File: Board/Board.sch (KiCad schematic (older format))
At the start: 40 parts, among them J1 5025700893, J2 Conn_01x02_Male, Q1 Q_NMOS_GSD, Q2 Q_NMOS_GSD, SW2 SW_SPST, U1 ATmega328P-AU, U2 TLV61225DCKR, Y1 10MHz

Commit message: Minor improvements
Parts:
- removed C4, C5: 18pF, Capacitor_SMD:C_0603_1608Metric, symbol Device:C
- removed R4: 3.48, Resistor_SMD:R_2512_6332Metric, symbol Device:R
- removed Y1: 10MHz, Crystal:Crystal_HC49-4H_Vertical, symbol Device:Crystal
- TP1, TP10, TP2, TP3, TP4, TP5, TP6, TP7, TP8, TP9: footprint TestPoint:TestPoint_THTPad_D1.0mm_Drill0.5mm -> Board:TestPoint_THTPad_D1.0mm_Drill0.7mm
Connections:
- net +3V3: no longer C6.1
- net +BATT: now also C6.1, LS1.1
- no-connect marks 13 -> 15
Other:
- moved on the sheet: C6, LS1, Q1, R3
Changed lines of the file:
@@
 L Device:Speaker LS1
 U 1 1 601143C0
-P 2150 5900
-F 0 "LS1" H 2320 5896 50  0000 L CNN
-F 1 "Speaker" H 2320 5805 50  0000 L CNN
-F 2 "Board:SPKR_CMS-151135-078S-67" H 2150 5700 50  0001 C CNN
-F 3 "~" H 2140 5850 50  0001 C CNN
-	1    2150 5900
+P 2150 5750
+F 0 "LS1" H 2320 5746 50  0000 L CNN
+F 1 "Speaker" H 2320 5655 50  0000 L CNN
+F 2 "Board:SPKR_CMS-151135-078S-67" H 2150 5550 50  0001 C CNN
+F 3 "~" H 2140 5700 50  0001 C CNN
+	1    2150 5750
 	1    0    0    -1
 $EndComp
@@
 $EndComp
 $Comp
-L Device:R R4
-U 1 1 6011E8C0
-P 1950 5600
-F 0 "R4" H 2020 5646 50  0000 L CNN
-F 1 "3.48" H 2020 5555 50  0000 L CNN
-F 2 "Resistor_SMD:R_2512_6332Metric" V 1880 5600 50  0001 C CNN
-F 3 "~" H 1950 5600 50  0001 C CNN
-	1    1950 5600
-	1    0    0    -1
-$EndComp
-$Comp
 L Device:C C6
 U 1 1 6011F8B1
-P 1800 5200
-F 0 "C6" V 1550 5150 50  0000 C CNN
-F 1 "1000uF" V 1650 5150 50  0000 C CNN
-F 2 "Capacitor_THT:C_Radial_D8.0mm_H11.5mm_P3.50mm" H 1838 5050 50  0001 C CNN
-F 3 "~" H 1800 5200 50  0001 C CNN
-	1    1800 5200
+P 1800 5400
+F 0 "C6" V 1550 5350 50  0000 C CNN
+F 1 "1000uF" V 1650 5350 50  0000 C CNN
+F 2 "Capacitor_THT:C_Radial_D8.0mm_H11.5mm_P3.50mm" H 1838 5250 50  0001 C CNN
+F 3 "~" H 1800 5400 50  0001 C CNN
+	1    1800 5400
 	0    1    1    0
 $EndComp
@@
 L power:GND #PWR01
 U 1 1 6012024F
-P 1650 5200
-F 0 "#PWR01" H 1650 4950 50  0001 C CNN
-F 1 "GND" V 1655 5072 50  0000 R CNN
-F 2 "" H 1650 5200 50  0001 C CNN
-F 3 "" H 1650 5200 50  0001 C CNN
-	1    1650 5200
-	0    1    1    0
-$EndComp
-$Comp
-L power:+3.3V #PWR02
-U 1 1 60120D4F
-P 1950 4900
-F 0 "#PWR02" H 1950 4750 50  0001 C CNN
-F 1 "+3.3V" H 1965 5073 50  0000 C CNN
-F 2 "" H 1950 4900 50  0001 C CNN
-F 3 "" H 1950 4900 50  0001 C CNN
-	1    1950 4900
-	1    0    0    -1
-$EndComp
-Wire Wire Line
-	1950 4900 1950 5200
-Wire Wire Line
-	1950 5200 1950 5450
-Connection ~ 1950 5200
-Wire Wire Line
-	1950 5750 1950 5900
+P 1650 5400
+F 0 "#PWR01" H 1650 5150 50  0001 C CNN
+F 1 "GND" V 1655 5272 50  0000 R CNN
+F 2 "" H 1650 5400 50  0001 C CNN
+F 3 "" H 1650 5400 50  0001 C CNN
+	1    1650 5400
+	0    1    1    0
+$EndComp
 $Comp
 L Device:Q_NMOS_GSD Q1
 U 1 1 60124F8A
-P 1850 6450
-F 0 "Q1" H 2054 6404 50  0000 L CNN
-F 1 "Q_NMOS_GSD" H 2054 6495 50  0000 L CNN
-F 2 "Package_TO_SOT_SMD:SOT-23" H 2050 6550 50  0001 C CNN
-F 3 "~" H 1850 6450 50  0001 C CNN
-	1    1850 6450
+P 1850 6300
+F 0 "Q1" H 2054 6254 50  0000 L CNN
+F 1 "Q_NMOS_GSD" H 2054 6345 50  0000 L CNN
+F 2 "Package_TO_SOT_SMD:SOT-23" H 2050 6400 50  0001 C CNN
+F 3 "~" H 1850 6300 50  0001 C CNN
+	1    1850 6300
 	1    0    0    1
 $EndComp
@@
 L Device:R R3
 U 1 1 601296B8
-P 1500 6450
-F 0 "R3" V 1300 6400 50  0000 L CNN
-F 1 "1k" V 1400 6400 50  0000 L CNN
-F 2 "Resistor_SMD:R_0603_1608Metric" V 1430 6450 50  0001 C CNN
-F 3 "~" H 1500 6450 50  0001 C CNN
-	1    1500 6450
-	0    1    1    0
-$EndComp
-Wire Wire Line
-	1350 6450 1000 6450
-Text Label 1000 6450 0    50   ~ 0
+P 1500 6300
+F 0 "R3" V 1300 6250 50  0000 L CNN
+F 1 "1k" V 1400 6250 50  0000 L CNN
+F 2 "Resistor_SMD:R_0603_1608Metric" V 1430 6300 50  0001 C CNN
+F 3 "~" H 1500 6300 50  0001 C CNN
+	1    1500 6300
+	0    1    1    0
+$EndComp
+Wire Wire Line
+	1350 6300 1000 6300
+Text Label 1000 6300 0    50   ~ 0
 SPEAKER
 $Comp
 L power:GND #PWR03
 U 1 1 6012AA28
-P 1950 6650
-F 0 "#PWR03" H 1950 6400 50  0001 C CNN
-F 1 "GND" H 1955 6477 50  0000 C CNN
-F 2 "" H 1950 6650 50  0001 C CNN
-F 3 "" H 1950 6650 50  0001 C CNN
-	1    1950 6650
-	1    0    0    -1
-$EndComp
-Wire Wire Line
-	1950 6000 1950 6250
+P 1950 6500
+F 0 "#PWR03" H 1950 6250 50  0001 C CNN
+F 1 "GND" H 1955 6327 50  0000 C CNN
+F 2 "" H 1950 6500 50  0001 C CNN
+F 3 "" H 1950 6500 50  0001 C CNN
+	1    1950 6500
+	1    0    0    -1
+$EndComp
+Wire Wire Line
+	1950 5850 1950 6100
 Wire Wire Line
 	9200 1950 9200 1750
@@
 F 0 "TP1" V 10150 4450 50  0000 L CNN
 F 1 "TestPoint" V 10150 4650 50  0000 L CNN
-F 2 "TestPoint:TestPoint_THTPad_D1.0mm_Drill0.5mm" H 10350 4250 50  0001 C CNN
+F 2 "Board:TestPoint_THTPad_D1.0mm_Drill0.7mm" H 10350 4250 50  0001 C CNN
 F 3 "~" H 10350 4250 50  0001 C CNN
 	1    10150 4250
@@
 F 0 "TP2" V 10150 4550 50  0000 L CNN
 F 1 "TestPoint" V 10150 4750 50  0000 L CNN
-F 2 "TestPoint:TestPoint_THTPad_D1.0mm_Drill0.5mm" H 10350 4350 50  0001 C CNN
+F 2 "Board:TestPoint_THTPad_D1.0mm_Drill0.7mm" H 10350 4350 50  0001 C CNN
 F 3 "~" H 10350 4350 50  0001 C CNN
 	1    10150 4350
@@
 F 0 "TP3" V 10150 5500 50  0000 L CNN
 F 1 "TestPoint" V 10150 5700 50  0000 L CNN
-F 2 "TestPoint:TestPoint_THTPad_D1.0mm_Drill0.5mm" H 10350 5300 50  0001 C CNN
+F 2 "Board:TestPoint_THTPad_D1.0mm_Drill0.7mm" H 10350 5300 50  0001 C CNN
 F 3 "~" H 10350 5300 50  0001 C CNN
 	1    10150 5300
@@
 F 0 "TP4" V 10150 5600 50  0000 L CNN
 F 1 "TestPoint" V 10150 5800 50  0000 L CNN
-F 2 "TestPoint:TestPoint_THTPad_D1.0mm_Drill0.5mm" H 10350 5400 50  0001 C CNN
+F 2 "Board:TestPoint_THTPad_D1.0mm_Drill0.7mm" H 10350 5400 50  0001 C CNN
 F 3 "~" H 10350 5400 50  0001 C CNN
 	1    10150 5400
@@
 F 0 "TP5" V 10150 5700 50  0000 L CNN
 F 1 "TestPoint" V 10150 5900 50  0000 L CNN
-F 2 "TestPoint:TestPoint_THTPad_D1.0mm_Drill0.5mm" H 10350 5500 50  0001 C CNN
+F 2 "Board:TestPoint_THTPad_D1.0mm_Drill0.7mm" H 10350 5500 50  0001 C CNN
 F 3 "~" H 10350 5500 50  0001 C CNN
 	1    10150 5500
@@
 F 0 "TP6" V 10150 5800 50  0000 L CNN
 F 1 "TestPoint" V 10150 6000 50  0000 L CNN
-F 2 "TestPoint:TestPoint_THTPad_D1.0mm_Drill0.5mm" H 10350 5600 50  0001 C CNN
+F 2 "Board:TestPoint_THTPad_D1.0mm_Drill0.7mm" H 10350 5600 50  0001 C CNN
 F 3 "~" H 10350 5600 50  0001 C CNN
 	1    10150 5600
@@
 F 0 "TP7" V 10150 5900 50  0000 L CNN
 F 1 "TestPoint" V 10150 6100 50  0000 L CNN
-F 2 "TestPoint:TestPoint_THTPad_D1.0mm_Drill0.5mm" H 10350 5700 50  0001 C CNN
+F 2 "Board:TestPoint_THTPad_D1.0mm_Drill0.7mm" H 10350 5700 50  0001 C CNN
 F 3 "~" H 10350 5700 50  0001 C CNN
 	1    10150 5700
@@
 F 0 "TP8" V 10150 6000 50  0000 L CNN
 F 1 "TestPoint" V 10150 6200 50  0000 L CNN
-F 2 "TestPoint:TestPoint_THTPad_D1.0mm_Drill0.5mm" H 10350 5800 50  0001 C CNN
+F 2 "Board:TestPoint_THTPad_D1.0mm_Drill0.7mm" H 10350 5800 50  0001 C CNN
 F 3 "~" H 10350 5800 50  0001 C CNN
 	1    10150 5800
 	0    1    1    0
 $EndComp
-Wire Wire Line
-	10000 2750 10100 2750
-Wire Wire Line
-	10000 2450 10100 2450
-Wire Wire Line
-	10400 2600 10400 2750
-Connection ~ 10400 2600
-$Comp
-L power:GND #PWR0107
-U 1 1 60122D93
-P 10400 2600
-F 0 "#PWR0107" H 10400 2350 50  0001 C CNN
-F 1 "GND" V 10405 2472 50  0000 R CNN
-F 2 "" H 10400 2600 50  0001 C CNN
-F 3 "" H 10400 2600 50  0001 C CNN
-	1    10400 2600
-	0    -1   -1   0
-$EndComp
-Wire Wire Line
-	10400 2450 10400 2600
-$Comp
-L Device:C C5
-U 1 1 60121939
-P 10250 2750
-F 0 "C5" V 10500 2750 50  0000 C CNN
-F 1 "18pF" V 10400 2750 50  0000 C CNN
-F 2 "Capacitor_SMD:C_0603_1608Metric" H 10288 2600 50  0001 C CNN
-F 3 "~" H 10250 2750 50  0001 C CNN
-	1    10250 2750
-	0    1    1    0
-$EndComp
-$Comp
-L Device:C C4
-U 1 1 60120E2F
-P 10250 2450
-F 0 "C4" V 9998 2450 50  0000 C CNN
-F 1 "18pF" V 10089 2450 50  0000 C CNN
-F 2 "Capacitor_SMD:C_0603_1608Metric" H 10288 2300 50  0001 C CNN
-F 3 "~" H 10250 2450 50  0001 C CNN
-	1    10250 2450
-	0    1    1    0
-$EndComp
-$Comp
-L Device:Crystal Y1
-U 1 1 6011255E
-P 10000 2600
-F 0 "Y1" V 10000 2450 50  0000 C CNN
-F 1 "10MHz" V 10000 2850 50  0000 C CNN
-F 2 "Crystal:Crystal_HC49-4H_Vertical" H 10000 2600 50  0001 C CNN
-F 3 "~" H 10000 2600 50  0001 C CNN
-	1    10000 2600
-	0    -1   -1   0
-$EndComp
-Connection ~ 10000 2750
-Wire Wire Line
-	9850 2750 10000 2750
-Connection ~ 10000 2450
-Wire Wire Line
-	9850 2450 10000 2450
-Wire Wire Line
-	9850 2550 9850 2450
-Wire Wire Line
-	9200 2550 9850 2550
-Wire Wire Line
-	9200 2650 9850 2650
-Wire Wire Line
-	9850 2650 9850 2750
 $Comp
 L power:GND #PWR012
@@
 F 0 "TP9" V 10150 3850 50  0000 L CNN
 F 1 "TestPoint" V 10150 4050 50  0000 L CNN
-F 2 "TestPoint:TestPoint_THTPad_D1.0mm_Drill0.5mm" H 10350 3650 50  0001 C CNN
+F 2 "Board:TestPoint_THTPad_D1.0mm_Drill0.7mm" H 10350 3650 50  0001 C CNN
 F 3 "~" H 10350 3650 50  0001 C CNN
 	1    10150 3650
@@
 F 0 "TP10" V 10150 3950 50  0000 L CNN
 F 1 "TestPoint" V 10150 4150 50  0000 L CNN
-F 2 "TestPoint:TestPoint_THTPad_D1.0mm_Drill0.5mm" H 10350 3750 50  0001 C CNN
+F 2 "Board:TestPoint_THTPad_D1.0mm_Drill0.7mm" H 10350 3750 50  0001 C CNN
 F 3 "~" H 10350 3750 50  0001 C CNN
 	1    10150 3750
@@
 	0    1    1    0
 $EndComp
+NoConn ~ 9200 2550
+NoConn ~ 9200 2650
+Wire Wire Line
+	1950 5400 1950 5750
+Wire Wire Line
+	1950 5400 1950 5050
+Connection ~ 1950 5400
+$Comp
+L power:+BATT #PWR02
+U 1 1 604DE421
+P 1950 5050
+F 0 "#PWR02" H 1950 4900 50  0001 C CNN
+F 1 "+BATT" H 1965 5223 50  0000 C CNN
+F 2 "" H 1950 5050 50  0001 C CNN
+F 3 "" H 1950 5050 50  0001 C CNN
+	1    1950 5050
+	1    0    0    -1
+$EndComp
 $EndSCHEMATC

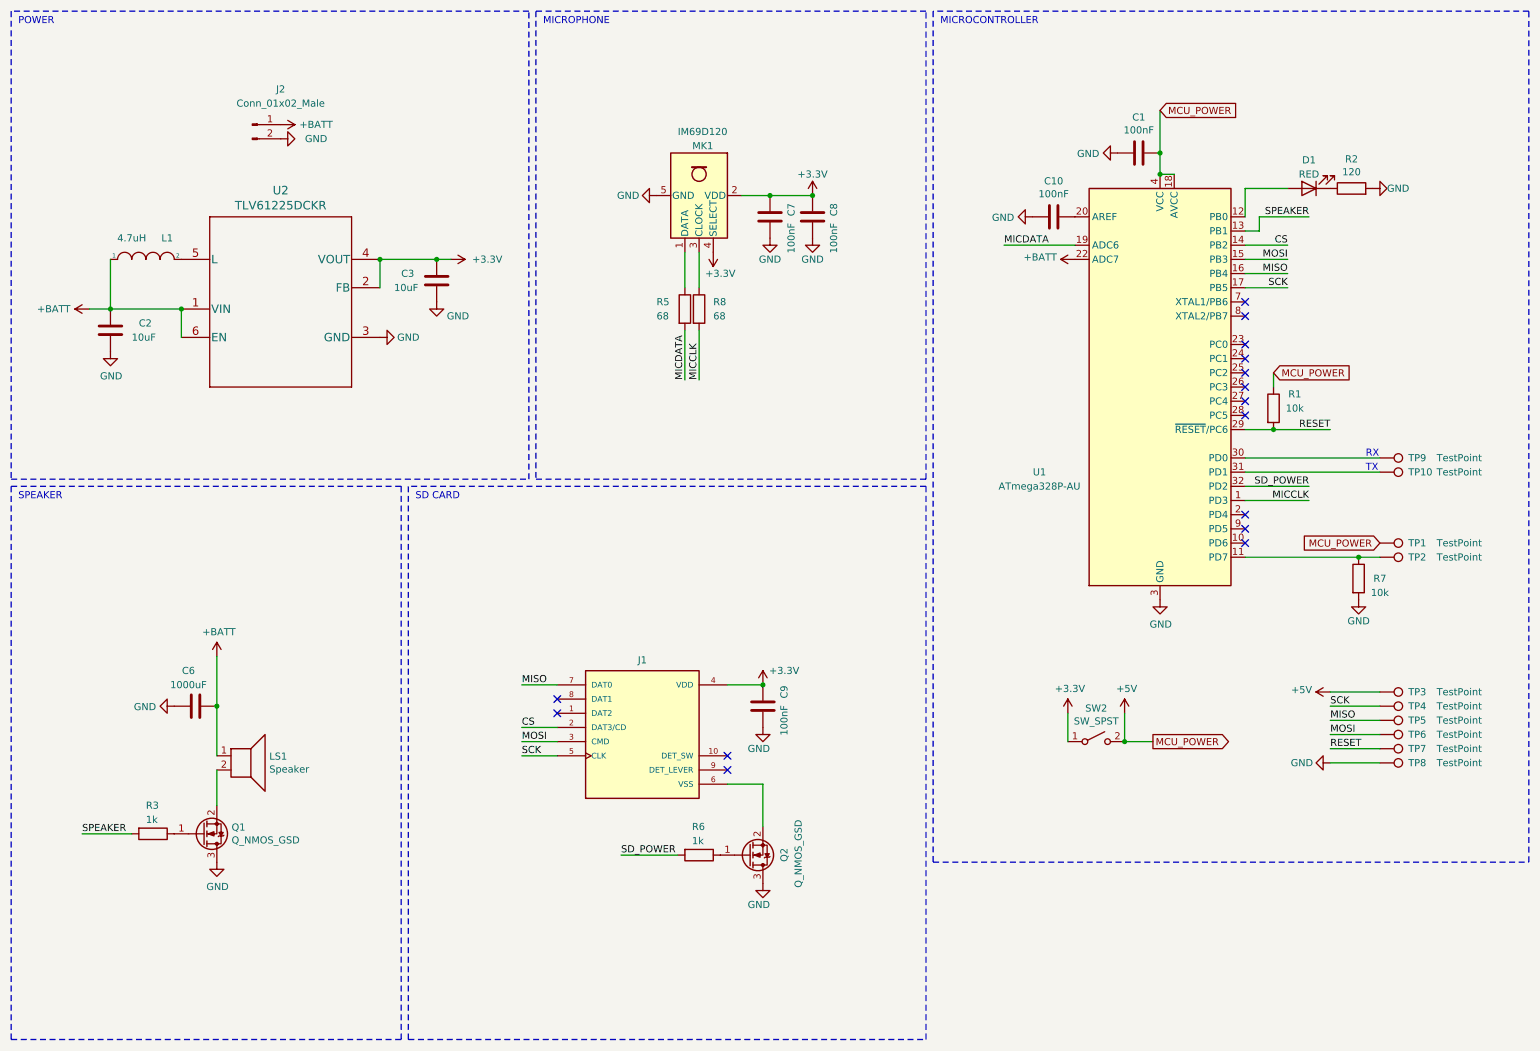
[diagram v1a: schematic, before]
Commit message: New microphone circuit
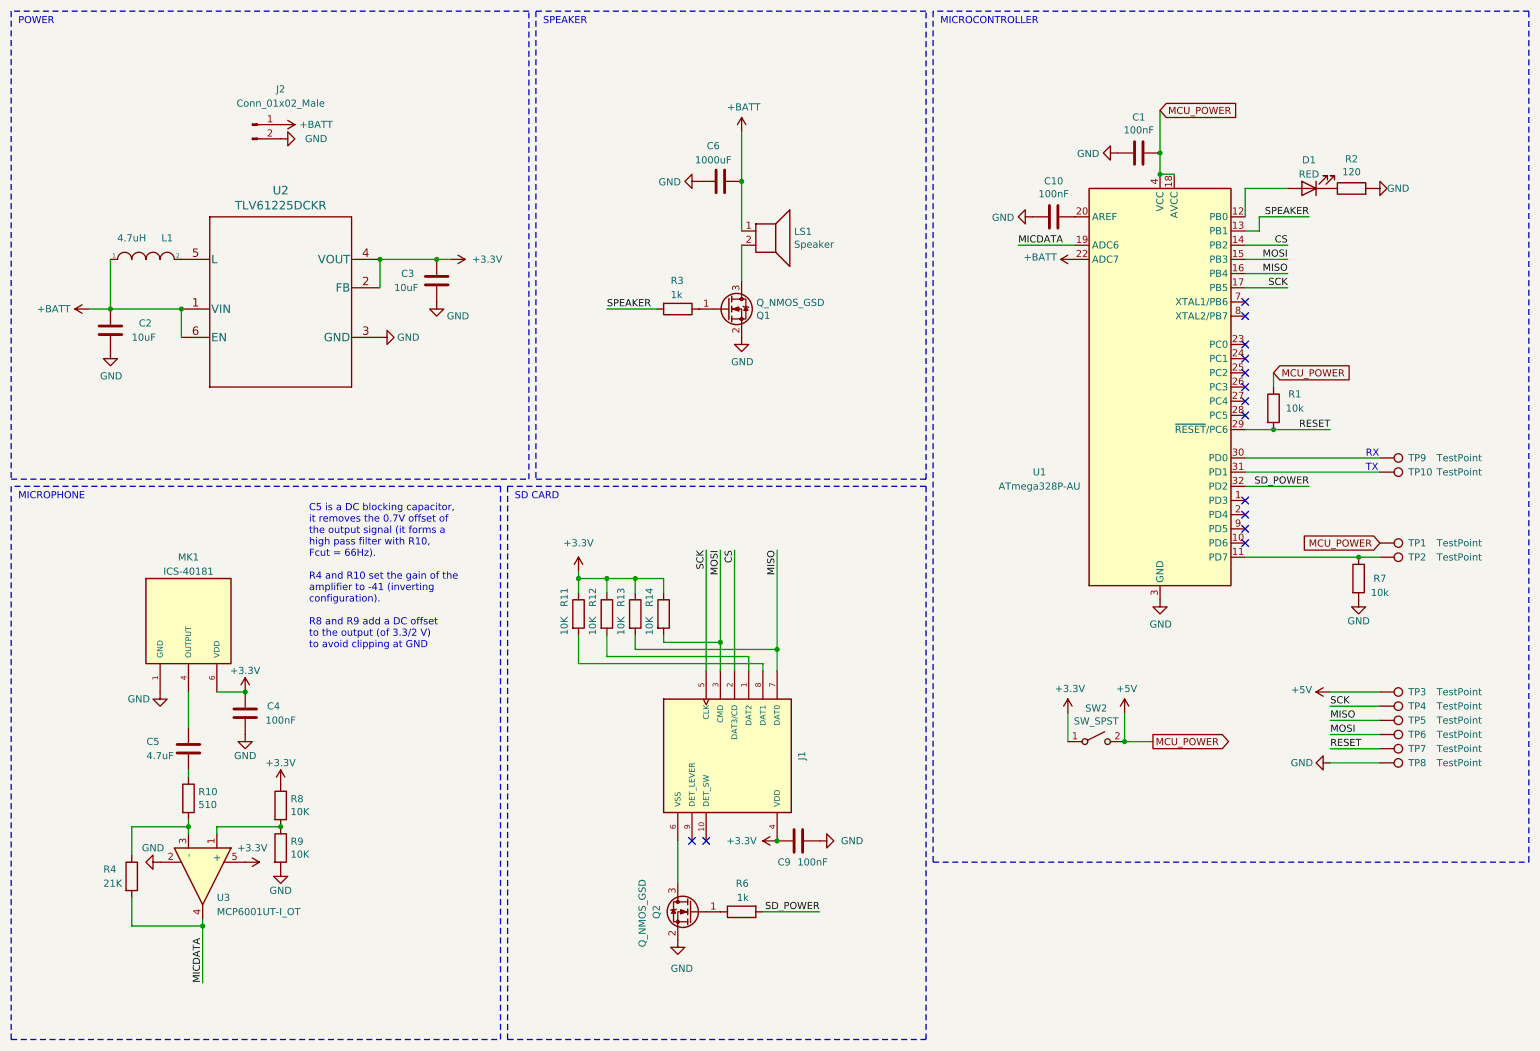
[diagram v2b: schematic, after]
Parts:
- removed C7, C8: 100nF, Capacitor_SMD:C_0603_1608Metric, symbol Device:C
- removed MK1: IM69D120, Sensor_Audio:Infineon_PG-LLGA-5-1, symbol Sensor_Audio:IM69D120
- removed R5: 68, Resistor_SMD:R_0603_1608Metric, symbol Device:R
- added C4: 100nF, Capacitor_SMD:C_0603_1608Metric, symbol Device:C
- added C5: 4.7uF, Capacitor_SMD:C_0603_1608Metric, symbol Device:C
- added MK1: ICS-40181, Board:MIC_ICS-40181, symbol Symbols:ICS-40181
- added R10: 510, Resistor_SMD:R_0603_1608Metric, symbol Device:R
- added R11, R12, R13, R14, R9: 10K, Resistor_SMD:R_0603_1608Metric, symbol Device:R
- added R4: 21K, Resistor_SMD:R_0603_1608Metric, symbol Device:R
- added U3: MCP6001UT-I_OT, Board:SOT95P270X145-5N, symbol Symbols:MCP6001UT-I_OT
- R8: value 68 -> 10K
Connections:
- net +3V3: now also R8.1, C4.1, MK1.6 (VDD), R11.1, R12.1, R13.1, R14.1, U3.5
- net GND: now also Q1.2 (S), Q2.2 (S), C4.2, MK1.1 (GND), MK1.2 (GND), MK1.3 (GND), MK1.5 (GND), R9.2, U3.2; no longer Q1.3 (D), Q2.3 (D)
- net MICDATA: now also R4.2, U3.4
- net MISO: now also R13.2
- net MOSI: now also R14.2
- net at LS1.2: now also Q1.3 (D); no longer Q1.2 (S)
- net at J1.6 (VSS): now also Q2.3 (D); no longer Q2.2 (S)
- net at J1.1 (DAT2): now also R12.2
- net at J1.8 (DAT1): now also R11.2
- net MICCLK: no longer names the net of U1.1 (PD3)
- net MICCLK: no longer R8.2
- new net: R8.2, R9.1, U3.1 (+)
- new net: R10.2, R4.1, U3.3 (-)
- new net: C5.1, MK1.4 (OUTPUT)
- new net: C5.2, R10.1
- no-connect marks 15 -> 14
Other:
- note added: "C5 is a DC blocking capacitor, \nit removes the 0.7V offset of \nthe output signal (it forms a \nhigh pass filter with R10, \nFcut = 66Hz).\n\nR4 and R10 set the gain of the\namplifier to -41 (inverting \nconfiguration).\n\nR8 and R9 add a DC offset \nto the output (of 3.3/2 V)\nto avoid clipping at GND"
- moved on the sheet: C6, C9, J1, LS1, Q1, Q2, R3, R6

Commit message: PCB v1.1 done
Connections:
- net MICDATA: now also U1.26 (PC3); no longer U1.19 (ADC6)
- net SD_POWER: now also U1.9 (PD5); no longer U1.32 (PD2)
- net at U1.12 (PB0): no longer D1.2 (A)
- net LED: now reaches U1.23 (PC0)
- net LED: now also D1.2 (A)
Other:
- moved on the sheet: D1, R2
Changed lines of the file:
@@
 L Device:LED D1
 U 1 1 60124EB0
-P 9650 1750
-F 0 "D1" H 9650 1550 50  0000 C CNN
-F 1 "RED" H 9650 1650 50  0000 C CNN
-F 2 "LED_SMD:LED_0805_2012Metric" H 9650 1750 50  0001 C CNN
-F 3 "~" H 9650 1750 50  0001 C CNN
-	1    9650 1750
-	-1   0    0    1
+P 10350 1600
+F 0 "D1" H 10350 1400 50  0000 C CNN
+F 1 "RED" H 10350 1500 50  0000 C CNN
+F 2 "LED_SMD:LED_0805_2012Metric" H 10350 1600 50  0001 C CNN
+F 3 "~" H 10350 1600 50  0001 C CNN
+	1    10350 1600
+	0    -1   -1   0
 $EndComp
 $Comp
 L Device:R R2
 U 1 1 6012AE91
-P 9950 1750
-F 0 "R2" V 10157 1750 50  0000 C CNN
-F 1 "120" V 10066 1750 50  0000 C CNN
-F 2 "Resistor_SMD:R_0603_1608Metric" V 9880 1750 50  0001 C CNN
-F 3 "~" H 9950 1750 50  0001 C CNN
-	1    9950 1750
-	0    -1   -1   0
+P 10350 1900
+F 0 "R2" V 10557 1900 50  0000 C CNN
+F 1 "120" V 10466 1900 50  0000 C CNN
+F 2 "Resistor_SMD:R_0603_1608Metric" V 10280 1900 50  0001 C CNN
+F 3 "~" H 10350 1900 50  0001 C CNN
+	1    10350 1900
+	1    0    0    -1
 $EndComp
 $Comp
 L power:GND #PWR0116
 U 1 1 6012AFF5
-P 10100 1750
-F 0 "#PWR0116" H 10100 1500 50  0001 C CNN
-F 1 "GND" V 10100 1650 50  0000 R CNN
-F 2 "" H 10100 1750 50  0001 C CNN
-F 3 "" H 10100 1750 50  0001 C CNN
-	1    10100 1750
-	0    -1   -1   0
+P 10350 2050
+F 0 "#PWR0116" H 10350 1800 50  0001 C CNN
+F 1 "GND" V 10350 1950 50  0000 R CNN
+F 2 "" H 10350 2050 50  0001 C CNN
+F 3 "" H 10350 2050 50  0001 C CNN
+	1    10350 2050
+	1    0    0    -1
 $EndComp
 $Comp
@@
 Wire Wire Line
 	5650 2150 5650 2400
-Wire Wire Line
-	9200 1950 9200 1750
 Wire Wire Line
 	9200 2050 9300 2050
@@
 NoConn ~ 9200 3350
 NoConn ~ 9200 3250
-NoConn ~ 9200 3150
 NoConn ~ 9200 3050
 NoConn ~ 9200 2950
-NoConn ~ 9200 2850
 Wire Wire Line
 	9800 5600 10150 5600
@@
 SD_POWER
 Wire Wire Line
-	9200 3850 9650 3850
-Text Label 9650 3850 2    50   ~ 0
+	9200 4150 9650 4150
+Text Label 9650 4150 2    50   ~ 0
 SD_POWER
-Wire Wire Line
-	9200 1750 9500 1750
 $Comp
 L power:GND #PWR0115
@@
 	10000 4350 9200 4350
 Connection ~ 10000 4350
-NoConn ~ 9200 4150
 NoConn ~ 9200 4250
 $Comp
@@
 $EndComp
 Wire Wire Line
-	8000 2150 7600 2150
-Text Label 7600 2150 0    50   ~ 0
-MICDATA
-Wire Wire Line
 	1950 5300 2150 5300
 $Comp
@@
 Wire Wire Line
 	1850 6950 1850 7350
+Wire Wire Line
+	9200 3150 9300 3150
+Wire Wire Line
+	9300 3150 9300 2950
+Wire Wire Line
+	9300 2950 9650 2950
+Text Label 9650 2950 2    50   ~ 0
+MICDATA
+NoConn ~ 8000 2150
+Wire Wire Line
+	10350 1450 10350 1150
+Text Label 10350 1150 3    50   ~ 0
+LED
+NoConn ~ 9200 1950
+Wire Wire Line
+	9200 2850 9650 2850
+Text Label 9650 2850 2    50   ~ 0
+LED
+NoConn ~ 9200 3850
 $EndSCHEMATC
